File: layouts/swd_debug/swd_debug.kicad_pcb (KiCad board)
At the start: 2 copper layers, 2 parts

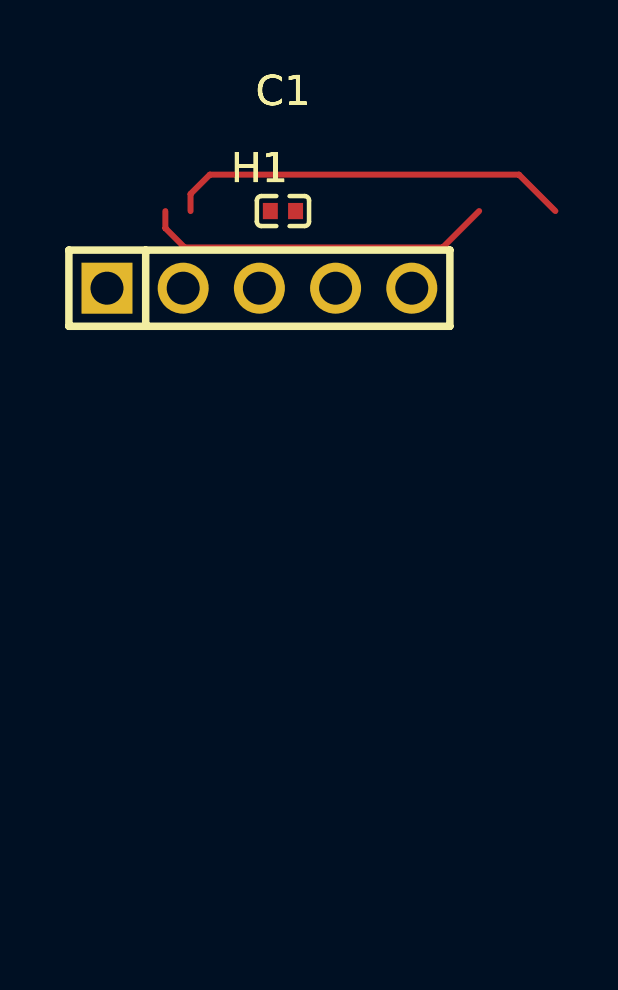
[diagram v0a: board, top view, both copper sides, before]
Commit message: Enhance smart placer with simulated annealing and pre-routing validation
Smart Placer improvements:
- Add simulated annealing refinement (now default) for better wire length optimization
- Add force-directed refinement with improvement safeguard
- Add silkscreen text repositioning to avoid component overlaps
- Significant wire length reductions (e.g., power_filter: 113mm -> 46mm)

Autorouter improvements:
- Add PreRoutingValidator class for pre-flight checks
- Validate unconnected pads, overlapping footprints, unplaced components
- Use pad-based bounds for accurate overlap detection
- Block routing on validation errors with actionable messages

Research:
- Add comprehensive autorouting/autoplacement findings document
- Cover Freerouting Python client, OrthoRoute, DeepPCB, KiCad 9 IPC API
- Document force-directed and simulated annealing algorithms

Cleanup:
- Update .gitignore for DSN/SES files, build artifacts, tools
- Remove stale timestamped build files
- Add parts footprints and symbols

All 10 modules placed and routed successfully.

Co-Authored-By: Claude Opus 4.5 <noreply@anthropic.com>
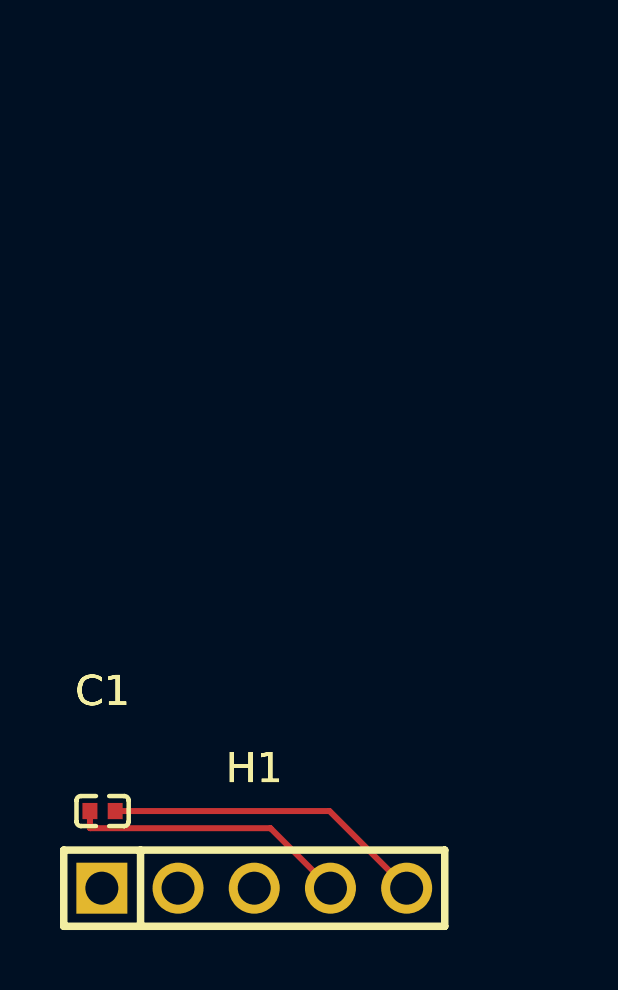
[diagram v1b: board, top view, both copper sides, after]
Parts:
- moved C1 20.9 mm to (94.0, 120.0)
- moved H1 20.0 mm to (99.0, 122.6)
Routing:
- net GND: track 13.5 -> 10.8 mm
- net SWD_RESET: track 11.8 -> 9.42 mm
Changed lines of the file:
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@@
 	(footprint "Samsung_Electro_Mechanics_CL05B104KO5NNNC:C0402"
 		(layer "F.Cu")
-		(at 100 100)
+		(at 93.9871 120)
 		(property "Reference" "C1"
 			(at 0 -4 0)
@@
 	(footprint "Ckmtw_B_2100S05P_A110:HDR-TH_5P-P2.54-V-M"
 		(layer "F.Cu")
-		(at 99.214177 102.57115)
+		(at 99.043 122.5711)
 		(property "Reference" "H1"
 			(at 0 -4 0)
@@
 	)
 	(segment
-		(start 96.08 100)
-		(end 96.08 100.5717)
+		(start 93.5671 120.5717)
+		(end 99.5836 120.5717)
 		(width 0.2)
 		(layer "F.Cu")
@@
 	)
 	(segment
-		(start 105.3265 101.2135)
-		(end 106.54 100)
+		(start 99.5836 120.5717)
+		(end 101.583 122.5711)
 		(width 0.2)
 		(layer "F.Cu")
@@
 	)
 	(segment
-		(start 96.08 100.5717)
-		(end 96.7218 101.2135)
+		(start 93.5671 120)
+		(end 93.5671 120.5717)
 		(width 0.2)
 		(layer "F.Cu")
@@
 	)
 	(segment
-		(start 96.7218 101.2135)
-		(end 105.3265 101.2135)
-		(width 0.2)
-		(layer "F.Cu")
-		(net 1)
-	)
-	(segment
-		(start 96.92 100)
-		(end 96.92 99.4283)
+		(start 104.123 122.5711)
+		(end 101.5519 120)
 		(width 0.2)
 		(layer "F.Cu")
@@
 	)
 	(segment
-		(start 96.92 99.4283)
-		(end 97.5619 98.7864)
+		(start 101.5519 120)
+		(end 94.4071 120)
 		(width 0.2)
 		(layer "F.Cu")
-		(net 4)
-	)
-	(segment
-		(start 97.5619 98.7864)
-		(end 107.8664 98.7864)
-		(width 0.2)
-		(layer "F.Cu")
-		(net 4)
-	)
-	(segment
-		(start 107.8664 98.7864)
-		(end 109.08 100)
-		(width 0.2)
-		(layer "F.Cu")
